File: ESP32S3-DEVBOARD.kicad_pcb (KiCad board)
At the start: 4 copper layers, 33 x 58.4 mm, 55 parts, among them J1 PinHeader_1x22_P2.54mm_Vertic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, J2 PinHeader_1x22_P2.54mm_Vertic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, J3 G-Switch_GT-USB-7010ASV, J4 G-Switch_GT-USB-7010ASV, Q1 BC817-40,215, Q2 BC817-40,215, SW1 TS-1088-AR02016, SW2 TS-1088-AR02016, SW3 TS-1088-AR02016, SW4 TS-1088-AR02016, SW5 SHOU_HAN_1.27-8P_TPPT, U1 AMS1117-3.3, U2 ESP32-S3-WROOM-1, U3 USBLC6-2P6, U4 CP2102N-A02-GQFN28R, U5 BMI270, U6 USBLC6-2P6

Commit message: finish componemt placement
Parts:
- removed C10: 100n, ESP32S3-DEVBOARD:C_0402_1005Metric
- J1, J2: moved to B.Cu
- moved C15 138.0 mm to (165.9, 148.3)
- moved C4 137.5 mm to (160.2, 148.3), turned to 180 degrees
- moved R1 135.3 mm to (157.3, 127.2)
- moved C14 134.2 mm to (165.9, 146.6)
- moved C3 133.0 mm to (160.3, 146.6), turned to 180 degrees
- moved R4 131.6 mm to (154.5, 130.5)
- moved R8 130.5 mm to (148.8, 140.3), turned to 180 degrees
- moved C5 128.2 mm to (155.8, 138.9), turned to 90 degrees
- moved R2 128.1 mm to (150.1, 127.8), turned to -90 degrees
- moved R5 128.0 mm to (152.5, 127.2)
- moved C6 124.8 mm to (157.0, 138.3), turned to 90 degrees
- moved R15 124.2 mm to (149.1, 131.7), turned to -90 degrees
- moved Q1 123.7 mm to (155.5, 128.3)
- moved R13 121.2 mm to (148.6, 127.9), turned to -90 degrees
- moved R14 121.1 mm to (148.6, 129.8), turned to 90 degrees
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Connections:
- J1 pad 3: /RST -> /EN
- SW5 pad 11: /GPIO6 -> +3.3V
- SW5 pad 12: /GPIO7 -> /GPIO6
- SW5 pad 13: +3.3V -> /GPIO7
- SW5 pad 4: /CSB_U5 -> /INT1
- SW5 pad 5: /INT1 -> /INT2
- SW5 pad 6: /INT2 -> /CSB_U5
- U4 pad 24: unconnected-(U4-~{RTS}-Pad24) -> /RTS
- U4 pad 28: unconnected-(U4-~{DTR}-Pad28) -> /DTR
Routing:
- net /GPIO12: track 33.8 -> 0.00 mm, vias 2 -> 0
- net /GPIO10: track 26.4 -> 0.00 mm, vias 2 -> 0
- net /GPIO11: track 26.2 -> 0.00 mm, vias 2 -> 0
- net /GPIO43: track 24.2 -> 0.00 mm, vias 2 -> 0
- net /GPIO9: track 23.4 -> 0.00 mm, vias 2 -> 0
- net /USB1_D-: track 21.9 -> 0.00 mm
- net /GPIO15: track 21.6 -> 0.00 mm, vias 1 -> 0
- net /GPIO46: track 21.4 -> 0.00 mm, vias 2 -> 0
- net /USB1_D+: track 20.2 -> 0.00 mm
- net /GPIO16: track 18.7 -> 0.00 mm, vias 1 -> 0
- net /GPIO8: track 17.8 -> 0.00 mm
- net /GPIO3: track 17.1 -> 0.00 mm, vias 2 -> 0
- net /GPIO18: track 16.7 -> 0.00 mm
- net GND: track 1.98 -> 17.7 mm, vias 2 -> 6
- net /GPIO17: track 15.4 -> 0.00 mm
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
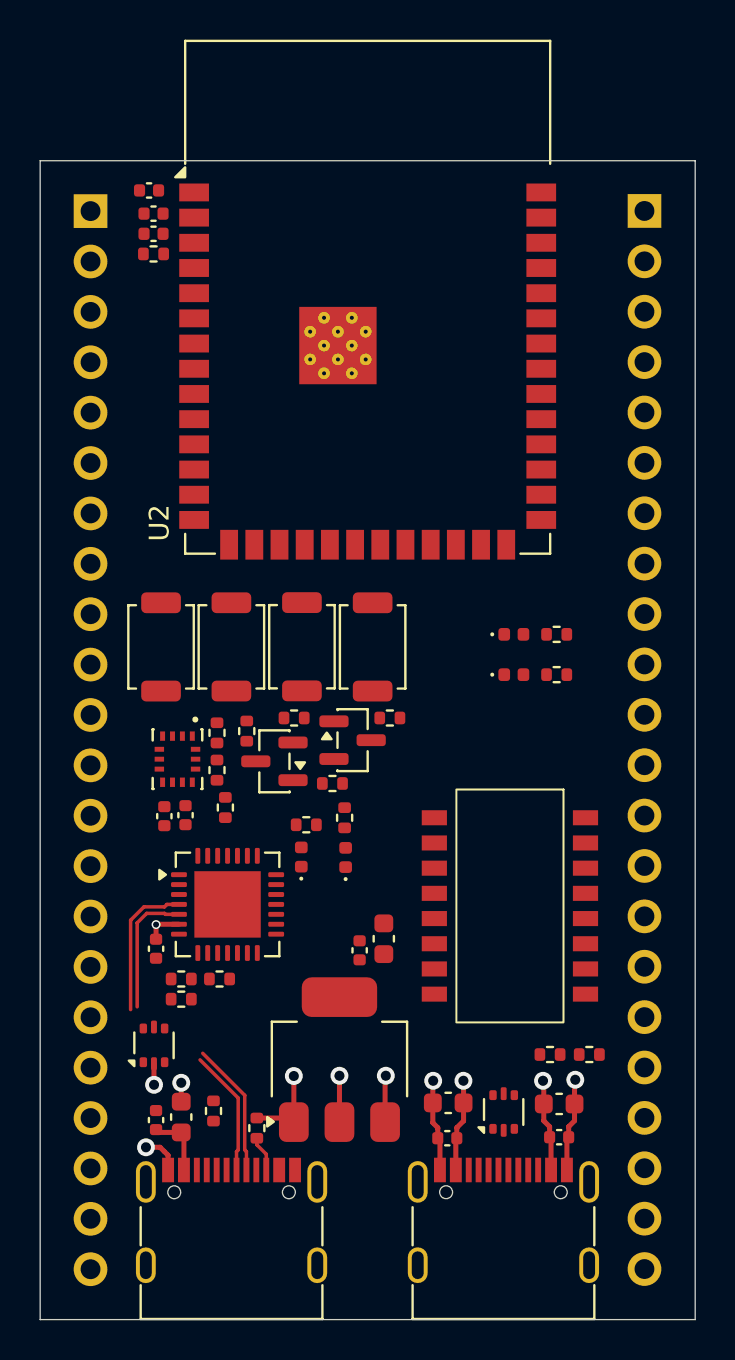
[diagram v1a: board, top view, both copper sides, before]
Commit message: fixed all errors (edit footprint silkskreens)
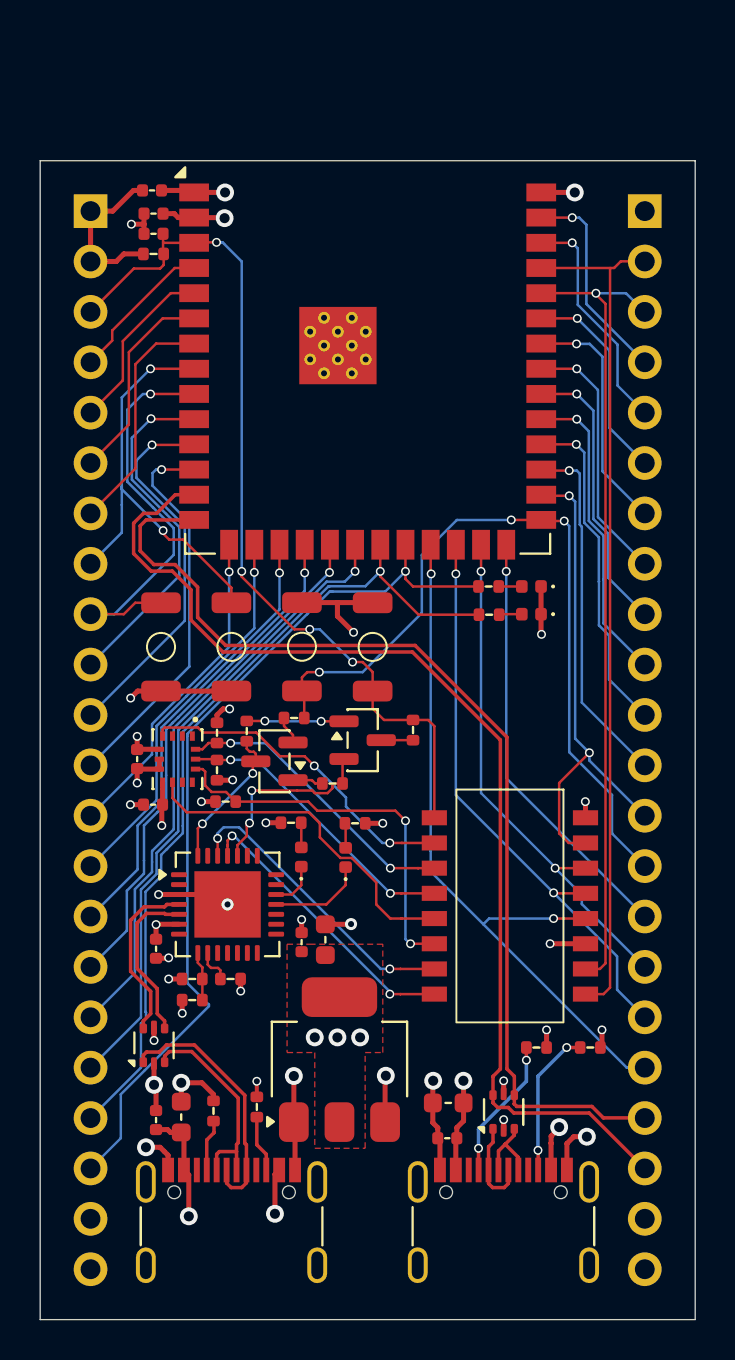
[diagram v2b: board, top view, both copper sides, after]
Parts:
- removed C14: 10u_{ 20%}, ESP32S3-DEVBOARD:C_0603_1608Metric
- removed C15: 100n, ESP32S3-DEVBOARD:C_0402_1005Metric
- J1, J2: footprint ESP32S3-DEVBOARD:PinHeader_1x22_P2.54mm_Vertical -> ESP32S3-DEVBOARD:PinHeader_1x22_P2.54mm_Vertical_FLIPPED; moved to F.Cu
- moved R20 4.55 mm to (162.3, 122.0), turned to 0 degrees
- moved D4 4.53 mm to (164.5, 120.5), turned to 180 degrees
- moved R21 4.19 mm to (162.3, 120.5), turned to 0 degrees
- moved C13 3.73 mm to (144.6, 129.2)
- moved C5 2.95 mm to (152.9, 138.5)
- moved C6 2.95 mm to (154.1, 138.3)
- moved D3 1.35 mm to (164.5, 121.9), turned to 180 degrees
- moved R1 1.32 mm to (158.5, 127.8), turned to 90 degrees
- moved R7 1.07 mm to (150.6, 146.8)
- moved C12 0.81 mm to (145.4, 131.5), turned to 180 degrees
- moved R11 0.77 mm to (152.4, 132.4)
- moved R16 0.77 mm to (164.7, 143.8)
- moved R12 0.60 mm to (155.6, 132.5), turned to 180 degrees
- moved R9 0.56 mm to (147.4, 141.4)
- moved R10 0.55 mm to (147.4, 140.3)
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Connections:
- SW5 pad 12: /GPIO6 -> /GPIO21
- SW5 pad 13: /GPIO7 -> /GPIO47
- SW5 pad 14: /GPIO4 -> /GPIO48
- SW5 pad 15: /GPIO5 -> /GPIO35
- SW5 pad 2: /I^{2}C_SDA -> /INT1
- SW5 pad 3: /I^{2}C_SCL -> /I^{2}C_SDA
- SW5 pad 4: /INT1 -> /I^{2}C_SCL
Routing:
- net /USB1_D-: track 0.00 -> 55.9 mm
- net /USB1_D+: track 0.00 -> 52.9 mm
- net /EN: track 0.00 -> 45.0 mm, vias 0 -> 4
- net /GPIO14: track 0.00 -> 44.7 mm, vias 0 -> 1
- net /GPIO43: track 0.00 -> 43.0 mm
- net /GPIO13: track 0.00 -> 42.1 mm, vias 0 -> 1
- net /GPIO44: track 0.00 -> 40.7 mm, vias 0 -> 1
- net /GPIO0: track 0.00 -> 39.4 mm, vias 0 -> 3
- net GND: track 17.7 -> 54.7 mm, vias 6 -> 26
- net /GPIO21: track 0.00 -> 36.6 mm, vias 0 -> 2
- net /GPIO12: track 0.00 -> 32.4 mm, vias 0 -> 1
- net /GPIO47: track 0.00 -> 29.3 mm, vias 0 -> 2
- net /GPIO11: track 0.00 -> 28.8 mm, vias 0 -> 1
- net /GPIO48: track 0.00 -> 26.7 mm, vias 0 -> 2
- net /GPIO10: track 0.00 -> 25.8 mm, vias 0 -> 1
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- added copper zone on F.Cu, net +3.3V
- added copper zone on In2.Cu, net +3.3V
- added copper zone on In2.Cu, net +5V
- added copper zone on In1.Cu, net GND

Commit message: Finnished the board!! :)
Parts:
- added G***: LOGO, LOGO, B.Cu at (156.2, 114.6)
- added G***: LOGO, LOGO, B.Cu at (159.9, 107.8)
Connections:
- net /LED_1 renamed /TX_LED
- net /LED_2 renamed /RX_LED
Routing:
- net GND: track 54.7 -> 56.6 mm
- net +3.3V: track 23.6 -> 25.4 mm
- net /GPIO14: track 44.7 -> 44.2 mm
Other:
- board text added: "+"
- board text added: "+3V"
- board text added: "+5V"
- board text added: "-"
- board text added: "0"
- board text added: "01"
- board text added: "02"
- board text added: "03"
- board text added: "04"
- board text added: "05"
- board text added: "06"
- board text added: "07"
- board text added: "08"
- board text added: "09"
- board text added: "10"
- board text added: "11"
- board text added: "12"
- board text added: "13"
- board text added: "14"
- board text added: "15"
- board text added: "16"
- board text added: "17"
- board text added: "18"
- board text added: "21"
- board text added: "35"
- board text added: "36"
- board text added: "37"
- board text added: "38"
- board text added: "39"
- board text added: "40"
- board text added: "41"
- board text added: "42"
- board text added: "43"
- board text added: "44"
- board text added: "45"
- board text added: "46"
- board text added: "47"
- board text added: "48"
- board text added: "DIP-SWITCH 1. EN 2. INT1 3. I^{2}C_SDA 4. I^{2}C_SCL 5. INT1 6. CSB 7. TX 8. RX"
- board text added: "Designed by Yaroslav Basiuk"
- board text added: "EN"
- board text added: "ESP32-S3 DevBoard"
- board text added: "GND"
- board text added: "R"
- board text added: "T"
- board text added: "buttons 15 16 B R"
- board text added: "l3-io13 l4-io14"
